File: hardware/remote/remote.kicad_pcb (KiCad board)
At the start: 2 copper layers, 106.7 x 86.4 mm, 30 parts

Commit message: hardware: Test all the input/output pins.
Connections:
- BUTTON1 pad 1: unconnected-(BUTTON1-S1_1-Pad1) -> Net-(BUTTON1-S1_1)
- BUTTON1 pad 3: Net-(BUTTON1-S2_1) -> unconnected-(BUTTON1-S2_1-Pad3)
- ESP32_UWB1 pad 18: Net-(BUTTON1-S2_1) -> Net-(ESP32_UWB1-IO35)
- ESP32_UWB1 pad 9: Net-(ESP32_UWB1-IO15) -> Net-(BUTTON1-S1_1)
- LOCK_SWITCH1 pad 2: Net-(BUTTON1-S1_2) -> Net-(ESP32_UWB1-IO14)
- LOCK_SWITCH1 pad 3: Net-(ESP32_UWB1-IO25) -> Net-(BUTTON1-S1_2)
- MINI_THUNSTICK1 pad 2: Net-(ESP32_UWB1-IO14) -> Net-(ESP32_UWB1-IO35)
- MINI_THUNSTICK1 pad 5: Net-(ESP32_UWB1-IO15) -> Net-(ESP32_UWB1-IO25)
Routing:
- net Net-(ESP32_UWB1-IO35): track 0.00 -> 46.3 mm
- net Net-(ESP32_UWB1-IO14): track 25.9 -> 7.18 mm
- net Net-(BUTTON1-S1_1): track 0.00 -> 17.0 mm
- net Net-(ESP32_UWB1-IO25): track 6.13 -> 21.1 mm
- net Net-(ESP32_UWB1-IO15): track 14.7 -> 0.00 mm
- net Net-(BUTTON1-S2_1): track 8.94 -> 0.00 mm
- net Net-(ESP32_UWB1-3V3): track 235.1 -> 231.1 mm
- net Net-(BUTTON1-S1_2): track 97.8 -> 100.6 mm
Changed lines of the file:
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@@
 	(net 14 "unconnected-(ESP32_UWB1-RST-Pad3)")
 	(net 15 "unconnected-(BUTTON2-S1_1-Pad1)")
-	(net 16 "Net-(ESP32_UWB1-IO15)")
+	(net 16 "unconnected-(BUTTON1-S2_1-Pad3)")
 	(net 17 "unconnected-(ON_OFF_SWITCH1-Pad1)")
 	(net 18 "unconnected-(ESP32_UWB1-IO18-Pad10)")
@@
 	(net 67 "Net-(BUTTON1-S1_2)")
 	(net 68 "unconnected-(BUTTON1-S2_2-Pad4)")
-	(net 69 "Net-(BUTTON1-S2_1)")
-	(net 70 "unconnected-(BUTTON1-S1_1-Pad1)")
+	(net 69 "Net-(BUTTON1-S1_1)")
+	(net 70 "Net-(ESP32_UWB1-IO35)")
 	(net 71 "unconnected-(ESP32_UWB1-IO34-Pad17)")
 	(net 72 "Net-(ESP32_UWB1-IO32)")
@@
 		(fp_line
 			(start 5.5 10.16)
+			(end 5.853553 10.513553)
+			(stroke
+				(width 0.1)
+				(type solid)
+			)
+			(layer "F.SilkS")
+		)
+		(fp_line
+			(start 5.5 10.16)
 			(end 5.853553 9.806447)
 			(stroke
@@
 			(layer "F.SilkS")
 		)
-		(fp_line
-			(start 5.5 10.16)
-			(end 5.853553 10.513553)
-			(stroke
-				(width 0.1)
-				(type solid)
-			)
-			(layer "User.4")
-		)
 		(fp_text user "Y"
 			(at 0 10.16 180)
@@
 			(layers "*.Cu" "*.Mask")
 			(remove_unused_layers no)
-			(net 57 "Net-(ESP32_UWB1-IO14)")
+			(net 70 "Net-(ESP32_UWB1-IO35)")
 			(pinfunction "X")
 			(pintype "power_in")
@@
 			(layers "*.Cu" "*.Mask")
 			(remove_unused_layers no)
-			(net 16 "Net-(ESP32_UWB1-IO15)")
+			(net 10 "Net-(ESP32_UWB1-IO25)")
 			(pinfunction "Y")
 			(pintype "output")
@@
 			(layers "*.Cu" "*.Mask")
 			(remove_unused_layers no)
-			(net 16 "Net-(ESP32_UWB1-IO15)")
+			(net 69 "Net-(BUTTON1-S1_1)")
 			(pinfunction "IO15")
 			(pintype "bidirectional")
@@
 			(layers "*.Cu" "*.Mask")
 			(remove_unused_layers no)
-			(net 69 "Net-(BUTTON1-S2_1)")
+			(net 70 "Net-(ESP32_UWB1-IO35)")
 			(pinfunction "IO35")
 			(pintype "bidirectional")
@@
 			(layers "*.Cu" "*.Mask")
 			(remove_unused_layers no)
-			(net 70 "unconnected-(BUTTON1-S1_1-Pad1)")
+			(net 69 "Net-(BUTTON1-S1_1)")
 			(pinfunction "S1_1")
 			(pintype "passive")
@@
 			(layers "*.Cu" "*.Mask")
 			(remove_unused_layers no)
-			(net 69 "Net-(BUTTON1-S2_1)")
+			(net 16 "unconnected-(BUTTON1-S2_1-Pad3)")
 			(pinfunction "S2_1")
 			(pintype "passive")
@@
 			(layers "*.Cu" "*.Mask")
 			(remove_unused_layers no)
-			(net 67 "Net-(BUTTON1-S1_2)")
+			(net 57 "Net-(ESP32_UWB1-IO14)")
 			(pintype "passive")
 		)
@@
 			(layers "*.Cu" "*.Mask")
 			(remove_unused_layers no)
-			(net 10 "Net-(ESP32_UWB1-IO25)")
+			(net 67 "Net-(BUTTON1-S1_2)")
 			(pintype "passive")
 		)
@@
 	)
 	(segment
-		(start 149.86 119.38)
-		(end 152.4 116.84)
+		(start 147.32 127)
+		(end 149.86 129.54)
 		(width 0.3)
 		(layer "F.Cu")
@@
 	)
 	(segment
-		(start 152.4 116.84)
+		(start 152.4 127)
 		(end 152.4 114.3)
 		(width 0.3)
@@
 	)
 	(segment
+		(start 147.32 125.82)
+		(end 147.32 127)
+		(width 0.3)
+		(layer "F.Cu")
+		(net 10)
+	)
+	(segment
+		(start 149.86 129.54)
+		(end 152.4 127)
+		(width 0.3)
+		(layer "F.Cu")
+		(net 10)
+	)
+	(segment
 		(start 110.49 66.04)
 		(end 105.41 66.04)
@@
 	)
 	(segment
-		(start 140.97 135.07)
-		(end 140.97 137.16)
-		(width 0.3)
-		(layer "F.Cu")
-		(net 12)
-	)
-	(segment
-		(start 153.871058 134.371058)
+		(start 138.52 132.62)
 		(end 145.32 125.82)
 		(width 0.3)
@@
 	)
 	(segment
-		(start 145.32 125.82)
-		(end 138.52 132.62)
-		(width 0.3)
-		(layer "F.Cu")
-		(net 12)
-	)
-	(segment
-		(start 176.69 134.371058)
-		(end 153.871058 134.371058)
-		(width 0.3)
-		(layer "F.Cu")
-		(net 12)
-	)
-	(segment
 		(start 133.35 68.58)
 		(end 135.89 66.04)
@@
 	)
 	(segment
-		(start 115.328942 132.08)
-		(end 106.68 123.431058)
+		(start 138.52 132.62)
+		(end 115.868942 132.62)
 		(width 0.3)
 		(layer "F.Cu")
@@
 	)
 	(segment
-		(start 138.43 139.7)
-		(end 130.81 132.08)
-		(width 0.3)
-		(layer "F.Cu")
-		(net 12)
-	)
-	(segment
-		(start 130.81 132.08)
-		(end 115.328942 132.08)
-		(width 0.3)
-		(layer "F.Cu")
-		(net 12)
-	)
-	(segment
 		(start 115.57 66.04)
 		(end 113.03 68.58)
@@
 	)
 	(segment
-		(start 140.97 137.16)
-		(end 138.43 139.7)
+		(start 123.19 68.58)
+		(end 120.65 66.04)
 		(width 0.3)
 		(layer "F.Cu")
@@
 	)
 	(segment
-		(start 123.19 68.58)
-		(end 120.65 66.04)
+		(start 115.868942 132.62)
+		(end 106.68 123.431058)
 		(width 0.3)
 		(layer "F.Cu")
@@
 	)
 	(segment
-		(start 138.52 132.62)
-		(end 140.97 135.07)
+		(start 175.26 124.46)
+		(end 146.68 124.46)
 		(width 0.3)
-		(layer "F.Cu")
+		(layer "B.Cu")
 		(net 12)
 	)
@@
 	)
 	(segment
+		(start 178.981058 132.08)
+		(end 178.981058 128.181058)
+		(width 0.3)
+		(layer "B.Cu")
+		(net 12)
+	)
+	(segment
 		(start 100.249 71.201)
 		(end 100.249 112.949)
@@
 	)
 	(segment
+		(start 176.69 134.371058)
+		(end 178.981058 132.08)
+		(width 0.3)
+		(layer "B.Cu")
+		(net 12)
+	)
+	(segment
+		(start 146.68 124.46)
+		(end 145.32 125.82)
+		(width 0.3)
+		(layer "B.Cu")
+		(net 12)
+	)
+	(segment
+		(start 178.981058 128.181058)
+		(end 175.26 124.46)
+		(width 0.3)
+		(layer "B.Cu")
+		(net 12)
+	)
+	(segment
 		(start 152.4 82.55)
 		(end 149.86 82.55)
@@
 	)
 	(segment
-		(start 147.32 125.82)
-		(end 142.24 120.74)
-		(width 0.3)
-		(layer "F.Cu")
-		(net 16)
-	)
-	(segment
-		(start 142.24 120.74)
-		(end 142.24 116.84)
-		(width 0.3)
-		(layer "F.Cu")
-		(net 16)
-	)
-	(segment
-		(start 142.24 116.84)
-		(end 144.78 114.3)
-		(width 0.3)
-		(layer "F.Cu")
-		(net 16)
-	)
-	(segment
 		(start 100.33 68.58)
 		(end 106.68 74.93)
@@
 	)
 	(segment
-		(start 137.16 134.62)
-		(end 138.52 134.62)
-		(width 0.3)
-		(layer "F.Cu")
-		(net 57)
-	)
-	(segment
-		(start 139.7 127)
-		(end 134.62 132.08)
-		(width 0.3)
-		(layer "F.Cu")
-		(net 57)
-	)
-	(segment
-		(start 134.62 132.08)
-		(end 137.16 134.62)
-		(width 0.3)
-		(layer "F.Cu")
-		(net 57)
-	)
-	(segment
 		(start 142.24 114.3)
-		(end 139.7 116.84)
-		(width 0.3)
-		(layer "F.Cu")
-		(net 57)
-	)
-	(segment
-		(start 139.7 116.84)
-		(end 139.7 127)
+		(end 147.32 119.38)
 		(width 0.3)
 		(layer "F.Cu")
@@
 	)
 	(segment
-		(start 161.26 129.291058)
-		(end 158.72 126.751058)
+		(start 149.86 119.38)
+		(end 149.86 125.28)
 		(width 0.3)
-		(layer "B.Cu")
+		(layer "F.Cu")
 		(net 67)
 	)
 	(segment
-		(start 157.788942 125.82)
-		(end 158.72 126.751058)
+		(start 149.86 125.28)
+		(end 149.32 125.82)
 		(width 0.3)
-		(layer "B.Cu")
+		(layer "F.Cu")
 		(net 67)
 	)
 	(segment
-		(start 176.69 129.291058)
-		(end 161.26 129.291058)
+		(start 161.26 129.291058)
+		(end 158.72 126.751058)
 		(width 0.3)
 		(layer "B.Cu")
@@
 	)
 	(segment
-		(start 135.86 126.751058)
-		(end 132.08 122.971058)
+		(start 157.788942 125.82)
+		(end 158.72 126.751058)
 		(width 0.3)
 		(layer "B.Cu")
@@
 	)
 	(segment
-		(start 138.791058 123.82)
-		(end 147.32 123.82)
+		(start 176.69 129.291058)
+		(end 161.26 129.291058)
 		(width 0.3)
 		(layer "B.Cu")
@@
 	)
 	(segment
-		(start 135.86 133.96)
-		(end 138.52 136.62)
+		(start 135.86 126.751058)
+		(end 132.08 122.971058)
 		(width 0.3)
 		(layer "B.Cu")
@@
 	)
 	(segment
-		(start 149.32 125.82)
-		(end 147.32 123.82)
+		(start 135.86 133.96)
+		(end 138.52 136.62)
+		(width 0.3)
+		(layer "B.Cu")
+		(net 67)
+	)
+	(segment
+		(start 138.52 136.62)
+		(end 149.32 125.82)
 		(width 0.3)
 		(layer "B.Cu")
@@
 	)
 	(segment
-		(start 147.32 123.82)
-		(end 147.32 119.38)
+		(start 149.32 119.92)
+		(end 149.86 119.38)
 		(width 0.3)
 		(layer "B.Cu")
@@
 	)
 	(segment
-		(start 135.86 126.751058)
-		(end 138.791058 123.82)
+		(start 158.72 121.671058)
+		(end 157.231058 121.671058)
 		(width 0.3)
 		(layer "B.Cu")
-		(net 67)
+		(net 69)
 	)
 	(segment
-		(start 171.42 121.671058)
-		(end 167.64 117.891058)
+		(start 147.32 116.84)
+		(end 144.78 114.3)
 		(width 0.3)
-		(layer "F.Cu")
+		(layer "B.Cu")
 		(net 69)
 	)
 	(segment
-		(start 167.64 117.891058)
+		(start 157.231058 121.671058)
+		(end 152.4 116.84)
+		(width 0.3)
+		(layer "B.Cu")
+		(net 69)
+	)
+	(segment
+		(start 152.4 116.84)
+		(end 147.32 116.84)
+		(width 0.3)
+		(layer "B.Cu")
+		(net 69)
+	)
+	(segment
+		(start 137.16 134.62)
+		(end 138.52 134.62)
+		(width 0.3)
+		(layer "F.Cu")
+		(net 70)
+	)
+	(segment
+		(start 160.02 134.62)
+		(end 167.64 127)
+		(width 0.3)
+		(layer "F.Cu")
+		(net 70)
+	)
+	(segment
+		(start 138.52 134.62)
+		(end 160.02 134.62)
+		(width 0.3)
+		(layer "F.Cu")
+		(net 70)
+	)
+	(segment
+		(start 167.64 127)
 		(end 167.64 114.3)
 		(width 0.3)
 		(layer "F.Cu")
-		(net 69)
+		(net 70)
 	)
 	(segment

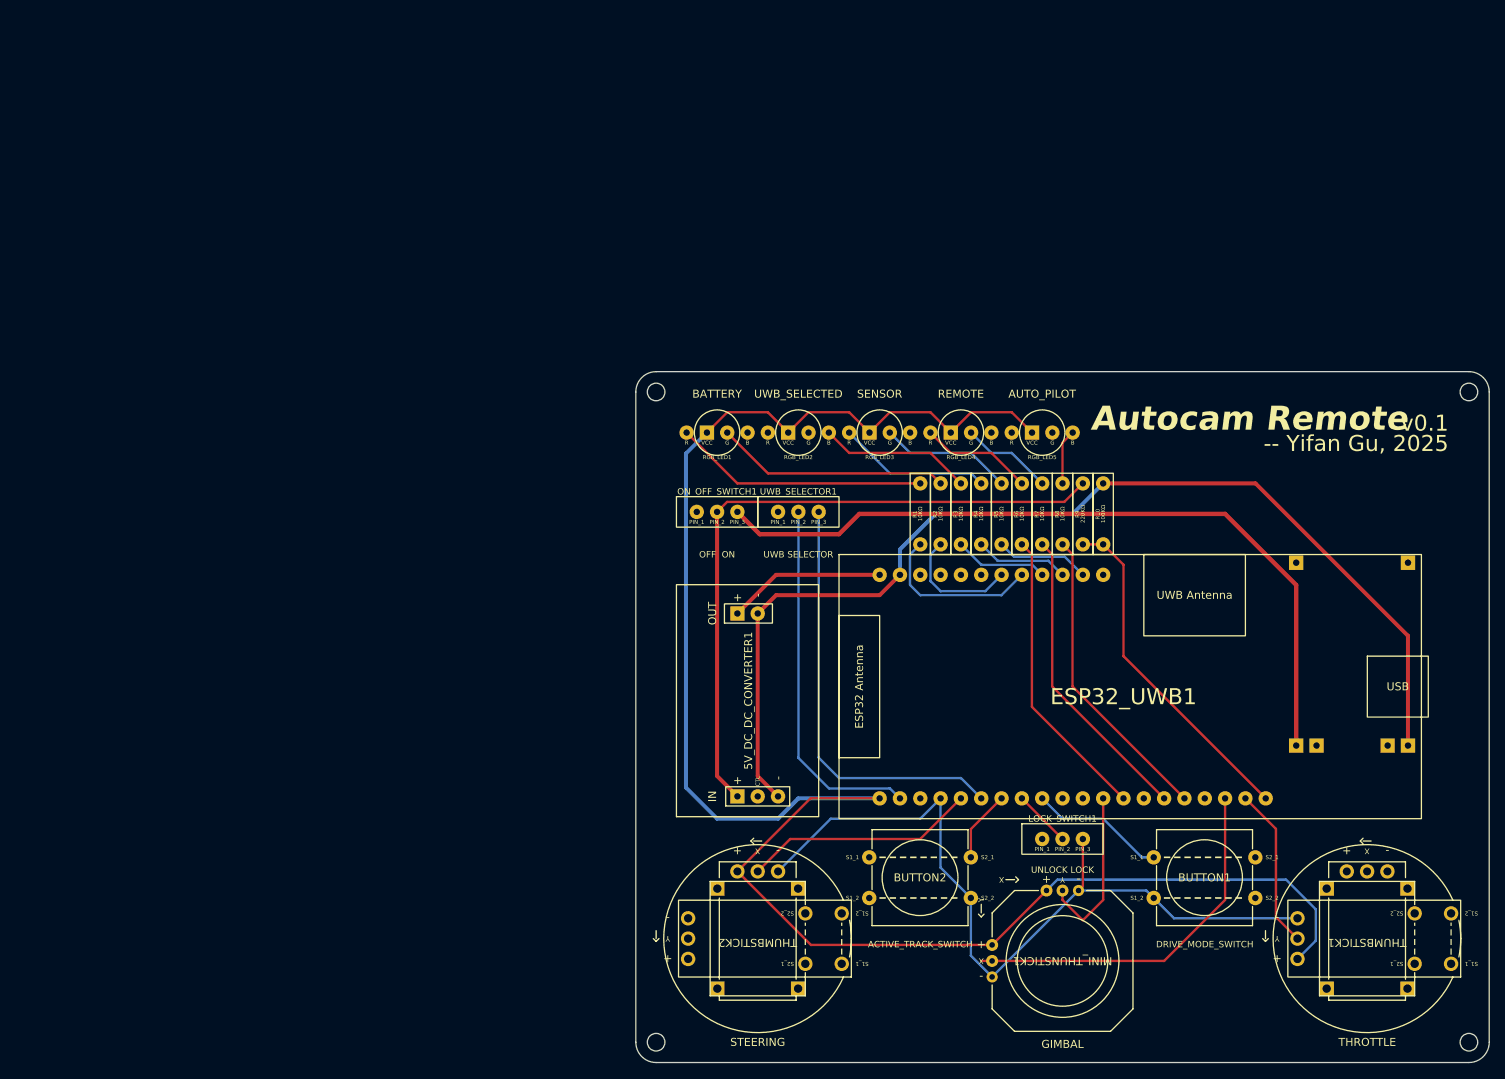
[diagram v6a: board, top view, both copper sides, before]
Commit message: hardware: Move the PCB to near the coordinate origin.
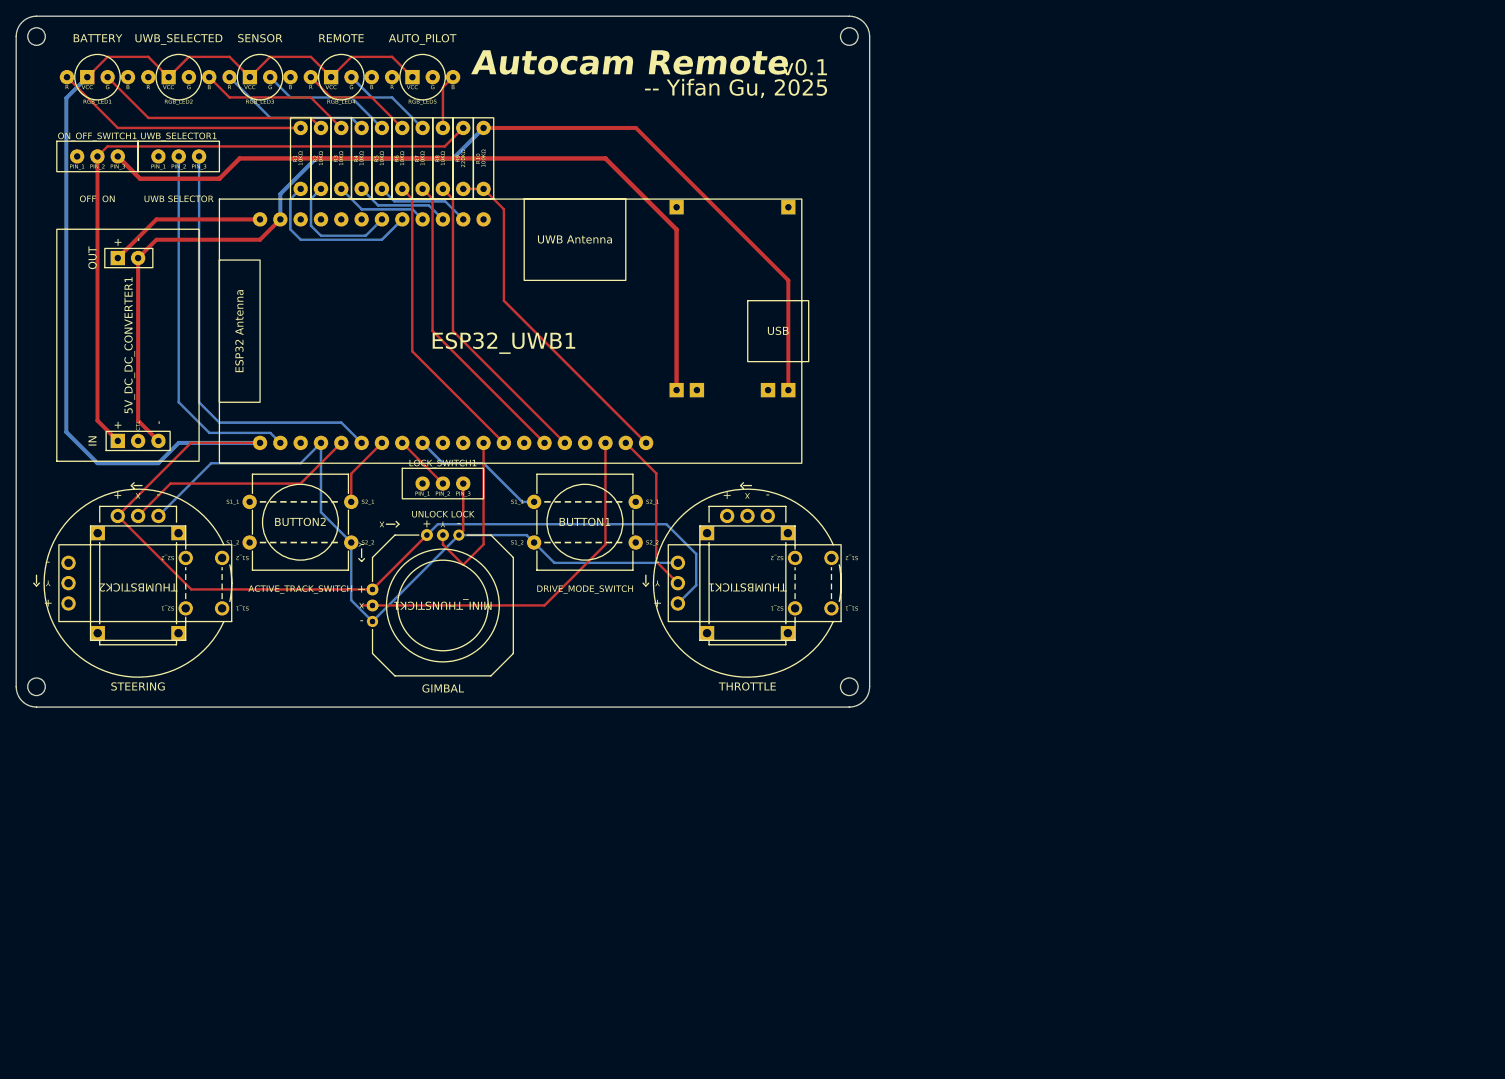
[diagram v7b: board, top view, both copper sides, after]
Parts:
- moved R2 89.3 mm to (54.6, 38.1)
- moved 3.7V_BATTERY_CHARGER1 89.3 mm to (114.8, 39.1)
- moved LOCK_SWITCH1 89.3 mm to (67.3, 74.9)
- moved MINI_THUNSTICK1 89.3 mm to (69.9, 90.2)
- moved R10 89.3 mm to (74.9, 38.1)
- moved R3 89.3 mm to (57.2, 38.1)
- moved R6 89.3 mm to (64.8, 38.1)
- moved R7 89.3 mm to (67.3, 38.1)
- moved R9 89.3 mm to (72.4, 38.1)
- moved REF** 89.3 mm to (120.7, 100.3)
- moved REF** 89.3 mm to (120.7, 19.1)
- moved RGB_LED4 89.3 mm to (57.2, 24.1)
- moved RGB_LED5 89.3 mm to (67.3, 24.1)
- moved THUMBSTICK1 89.3 mm to (107.9, 87.4)
- moved THUMBSTICK2 89.3 mm to (31.8, 87.4)
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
